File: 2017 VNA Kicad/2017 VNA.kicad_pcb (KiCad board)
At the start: 2 copper layers, 50 x 30 mm, 49 parts, among them P1 Output, P2 Input, U1 SI5351A, U2 NL7WB66, U3 NL7WB66, Y1 CX3225

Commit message: New PCB spin.
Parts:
- removed G***: Launchpad_LOGO_small, kilibs:Launchpad_LOGO_small
- removed G***: LOGO, EtherkitKicadLibrary:OSHWLogo4mm
- removed SHIELD1, SHIELD2: BMI-S-202-F, kilibs:LAIRD-BMI-S-202
- added ?: , RPi_Hat:RPi_Hat_Mounting_Hole, F.Cu at (111.5, 172.4)
- added ?: , RPi_Hat:RPi_Hat_Mounting_Hole, F.Cu at (111.5, 123.4)
- added ?: , RPi_Hat:RPi_Hat_Mounting_Hole, F.Cu at (53.5, 123.4)
- added ?: , RPi_Hat:RPi_Hat_Mounting_Hole, F.Cu at (53.5, 172.4)
- added A1: Arduino_Nano_v3.x, Modules:Arduino_Nano, F.Cu at (69.0, 144.0)
- added C11: 0.1uF, Capacitors_SMD:C_0805, F.Cu at (56.7, 148.3)
- added C18: 0.1uF, Capacitors_SMD:C_0805, F.Cu at (64.6, 129.5)
- added J1: AudioJack3, 2017 VNA Kicad:Tayda_3.5mm_stereo_TRS_jack_A-853, F.Cu at (56.0, 133.0)
- added J2: RF_Shield_Two_Pieces, kilibs:LAIRD-BMI-S-202, F.Cu at (65.0, 168.0)
- added J3: Raspberry_Pi_2_3, Pin_Headers:Pin_Header_Straight_2x20_Pitch2.54mm, F.Cu at (58.4, 124.7)
- added J4: RF_Shield_Two_Pieces, kilibs:LAIRD-BMI-S-202, F.Cu at (83.0, 168.0)
- added TX1: LO_Q, Connectors:PINTST, F.Cu at (48.2, 169.1)
- added U4: LM2904, 2017 VNA Kicad:SOIC-8, F.Cu at (83.0, 136.3)
- R3: value 56 -> 47
- moved U2 82.4 mm to (53.8, 162.6), turned to 0 degrees
- moved U3 77.5 mm to (111.6, 162.6), turned to 90 degrees
- moved B1 76.8 mm to (83.5, 148.4)
- moved C10 76.8 mm to (88.9, 159.8)
- moved C12 76.8 mm to (67.8, 156.8)
- moved C13 76.8 mm to (85.7, 154.6)
- moved C14 76.8 mm to (74.1, 156.1)
- moved C15 76.8 mm to (88.5, 153.1)
- moved C16 76.8 mm to (71.6, 152.8)
- moved C4 76.8 mm to (95.3, 164.9)
- moved C8 76.8 mm to (67.8, 162.3)
- moved CLK1 76.8 mm to (79.3, 165.0)
- moved IN1 76.8 mm to (97.7, 164.7)
- moved L1 76.8 mm to (67.7, 165.4)
- moved L2 76.8 mm to (87.7, 164.5)
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- renumbered LO_Q1 to CLK1
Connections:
- B1 pad 5V: (no net) -> +5V
- C1 pad 2: /Ref_In -> /TX
- C15 pad 1: Net-(B1-PadP5.1) -> Net-(C15-Pad1)
- C16 pad 1: Net-(B1-PadP4.7) -> Net-(C16-Pad1)
- C5 pad 1: +3V3 -> GND
- C5 pad 2: GND -> +3V3
- CLK1 pad 1: /LO_Q -> /Ref_In
- R15 pad 1: Net-(B1-PadP4.7) -> Net-(C16-Pad1)
- R8 pad 1: Net-(B1-PadP5.1) -> Net-(C15-Pad1)
- U1 pad 10: /Ref_In -> /TX
- U1 pad 9: /LO_Q -> /Ref_In
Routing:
- net +3V3: track 102.8 -> 79.4 mm
- net /TX: track 0.00 -> 15.1 mm
- net /Ref_In: track 15.1 -> 3.46 mm
- net Net-(B1-PadP5.1): track 21.2 -> 9.81 mm
- net GND: track 544.7 -> 535.0 mm, vias 196 -> 192
- net /SDA: track 46.8 -> 38.5 mm
- net /SCL: track 47.8 -> 40.9 mm
- net /LO_Q: track 3.46 -> 0.00 mm
- net Net-(B1-PadP4.7): track 21.6 -> 18.9 mm
- net /LO_I: vias 2 -> 3
- net Net-(C9-Pad1): vias 2 -> 3
- net (no net): vias 4 -> 5
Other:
- board size 50 x 30 mm -> 65 x 56 mm
- board text added: "Camera Flex Slot (Optional)"
- board text added: "Dimensions taken from https://github.com/raspberrypi/hats/blob/master/hat-board-mechanical.pdf"

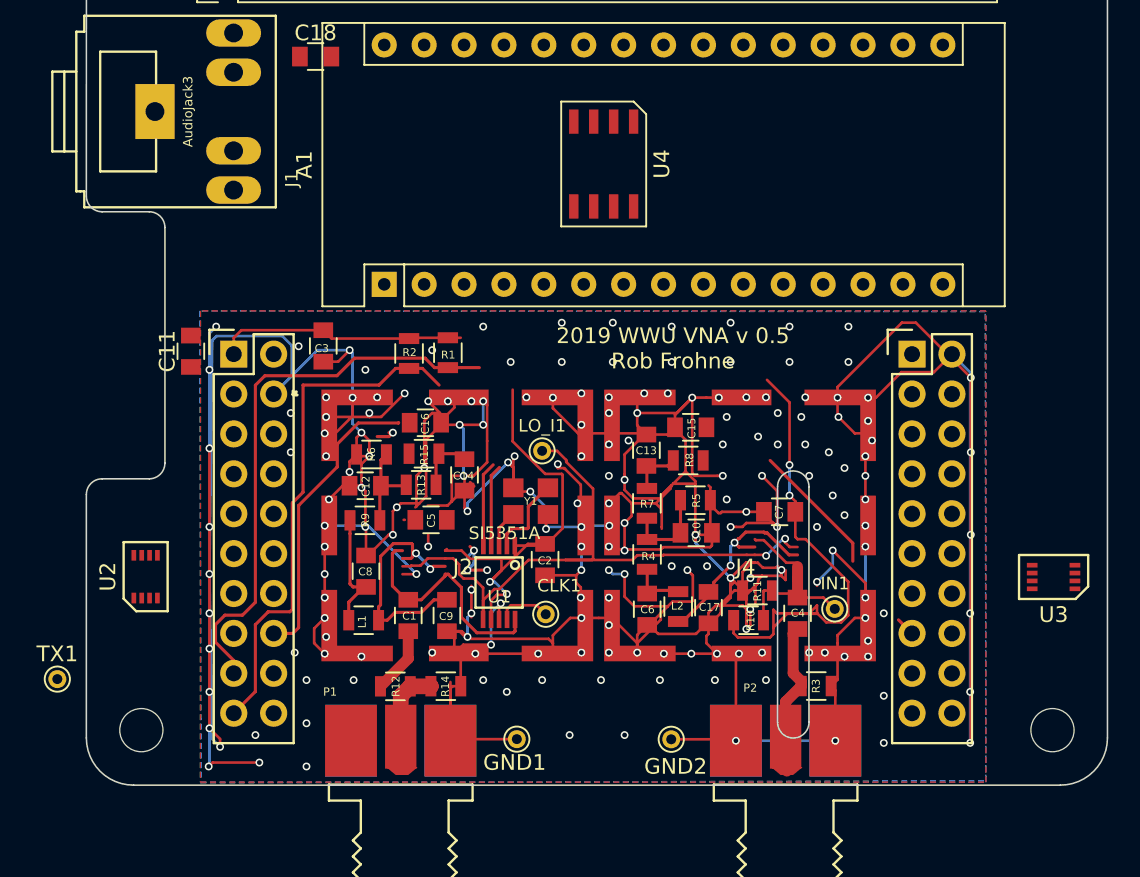
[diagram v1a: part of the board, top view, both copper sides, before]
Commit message: Added the footprint for the 3.5mm connector.
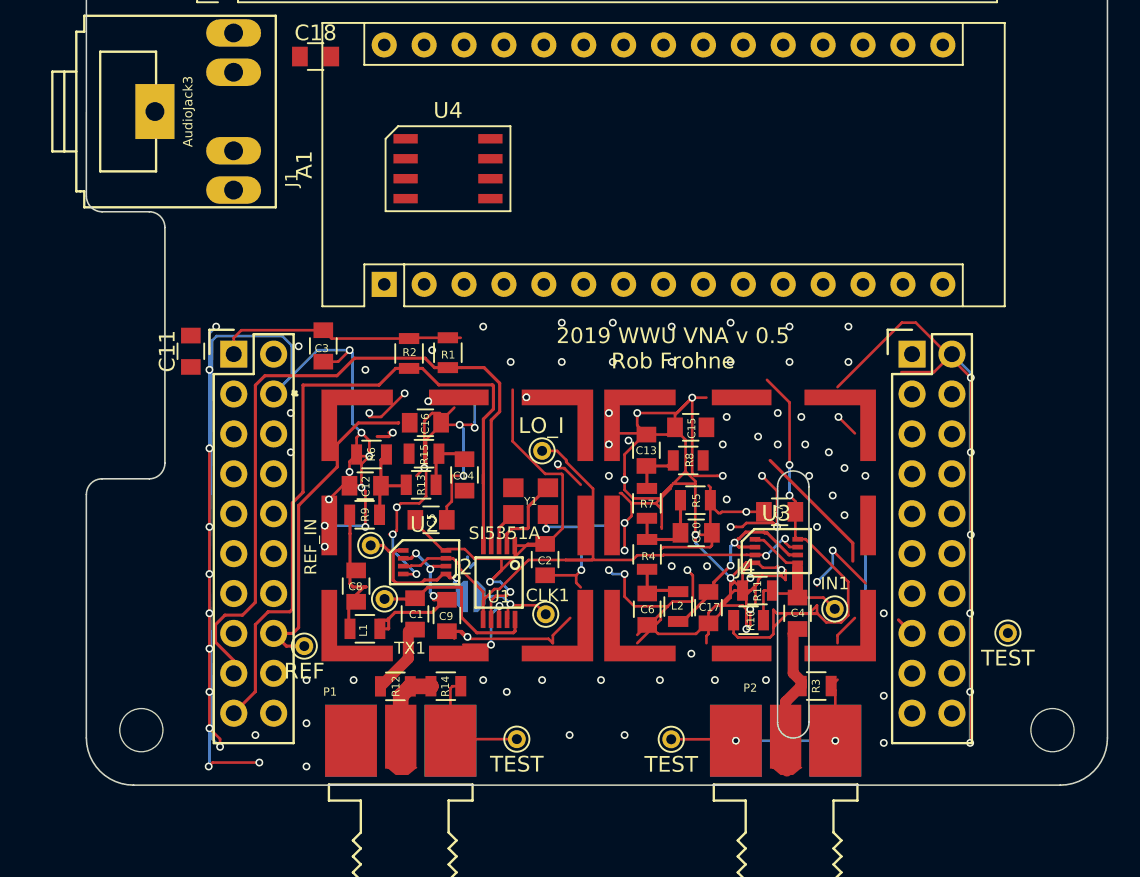
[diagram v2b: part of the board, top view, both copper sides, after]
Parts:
- added JP1: Jumper, EtherkitKicadLibrary:SOLDER_JUMPER, B.Cu at (74.5, 163.9)
- added TP1: REF_IN, Connectors:PINTST, F.Cu at (68.1, 160.6)
- added TP2: REF, Connectors:PINTST, F.Cu at (63.9, 167.0)
- added TP3: TEST, Connectors:PINTST, F.Cu at (108.7, 166.2)
- moved TX1 21.4 mm to (69.0, 164.0)
- moved U2 17.8 mm to (71.6, 161.7), turned to 270 degrees
- moved U3 17.7 mm to (94.0, 161.0), turned to 270 degrees
- moved U4 9.91 mm to (73.1, 136.6), turned to 270 degrees
- moved C8 1.14 mm to (67.2, 163.2)
- moved L1 0.55 mm to (67.8, 165.9)
- moved C1 0.44 mm to (71.0, 165.0)
- moved R9 0.35 mm to (67.8, 158.7)
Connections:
- CLK1 pad 1: /Ref_In -> Net-(CLK1-Pad1)
- J1 pad 1: (no net) -> GND
- J1 pad 2: (no net) -> Net-(B1-PadP5.1)
- J1 pad 3: (no net) -> Net-(B1-PadP4.7)
- U1 pad 9: /Ref_In -> Net-(CLK1-Pad1)
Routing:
- net GND: track 535.0 -> 411.0 mm, vias 192 -> 125
- net /SDA: track 38.5 -> 47.5 mm
- net /Ref_In: track 3.46 -> 10.8 mm, vias 0 -> 1
- net /SCL: track 40.9 -> 48.0 mm
- net Net-(CLK1-Pad1): track 0.00 -> 5.87 mm, vias 0 -> 1
- net (no net): track 5.05 -> 1.76 mm, vias 5 -> 2
- net +3V3: track 79.4 -> 82.6 mm
- net Net-(C9-Pad1): track 15.5 -> 12.6 mm
- net /TX: track 15.1 -> 12.8 mm
- net Net-(B1-PadP4.7): track 18.9 -> 21.2 mm
- net /LO_I: track 42.3 -> 41.9 mm, vias 3 -> 2
- removed copper zone on B.Cu, net GND
- removed copper zone on F.Cu, net GND

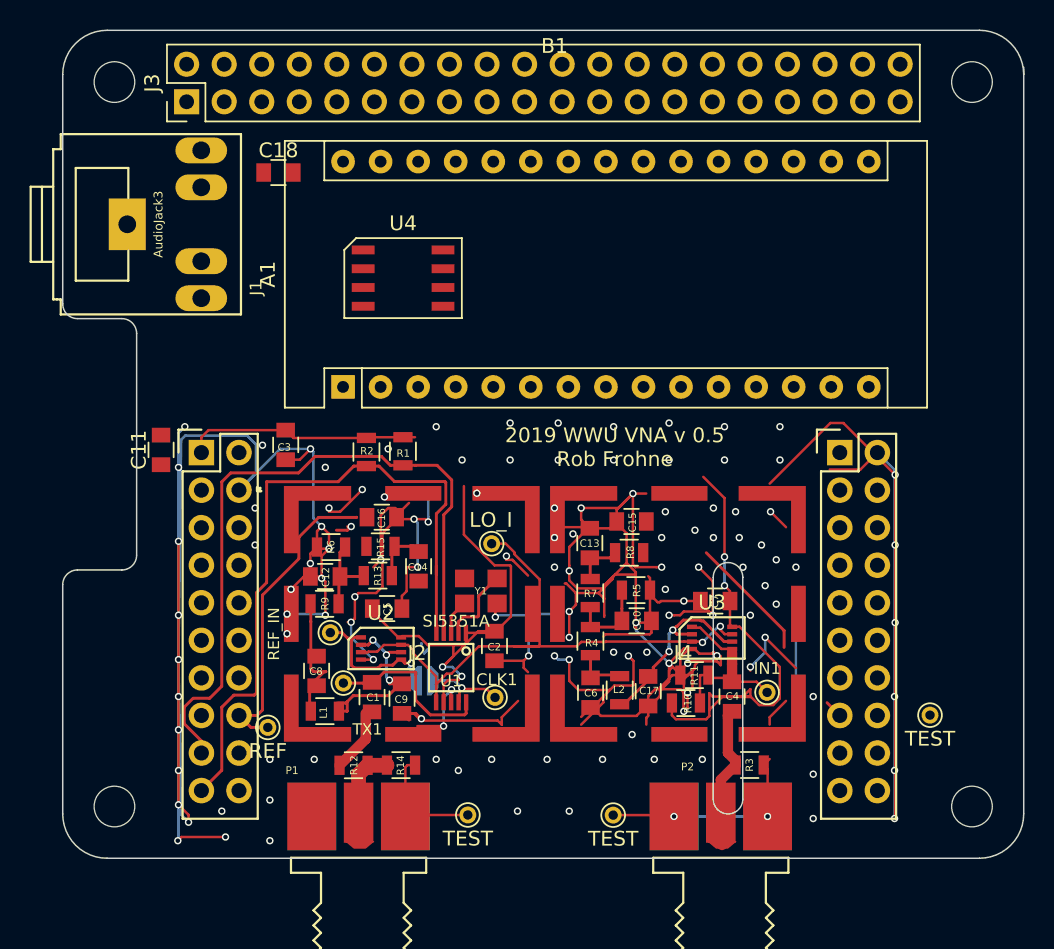
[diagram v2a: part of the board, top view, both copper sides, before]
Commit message: Added v0.51 to the Kicad directory.
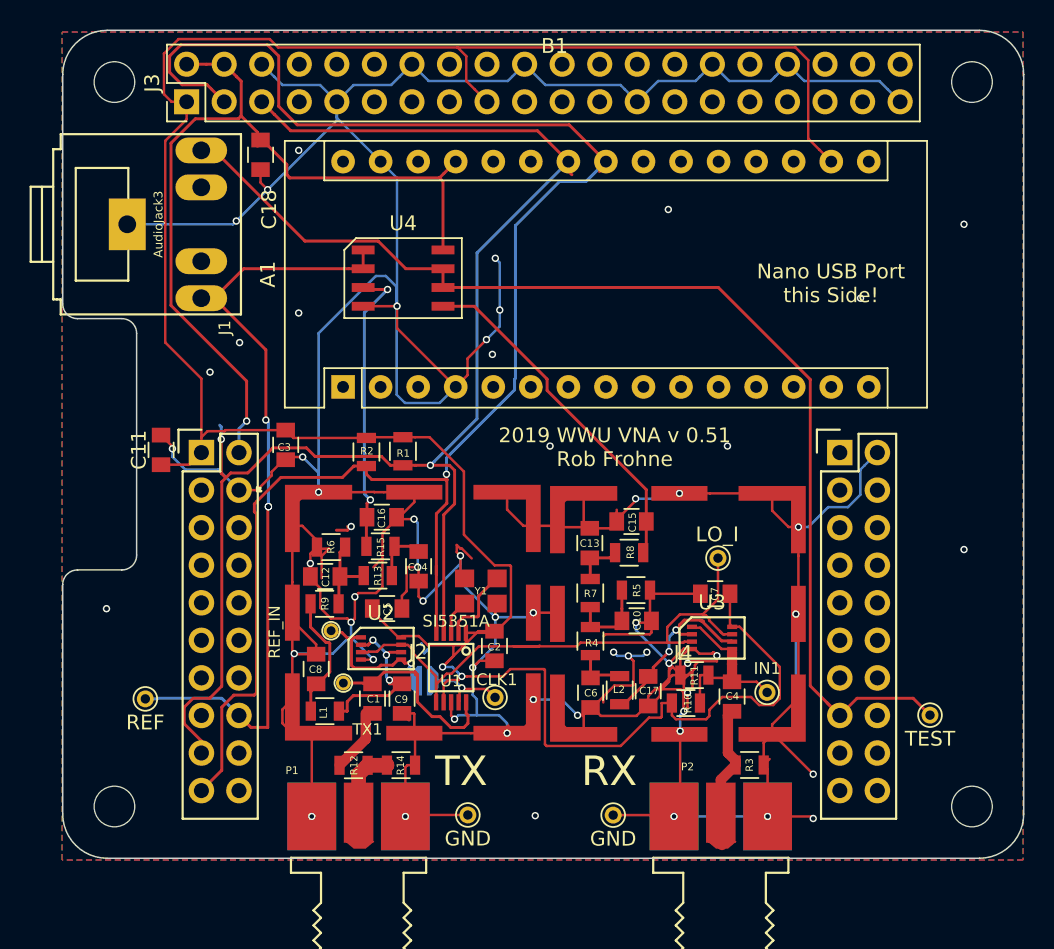
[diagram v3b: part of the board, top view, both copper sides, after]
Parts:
- GND1, GND2: value TEST -> GND
- moved LO_I1 15.3 mm to (94.4, 155.6)
- moved TP2 8.51 mm to (55.6, 165.1)
- moved C18 1.70 mm to (63.4, 128.3), turned to 270 degrees
- moved C7 0.49 mm to (94.2, 158.0)
- moved TP1 0.14 mm to (68.2, 160.5)
- moved C8 0.13 mm to (67.2, 163.1)
- moved J2 0.11 mm to (65.1, 167.9)
- moved C1 0.10 mm to (71.0, 165.1)
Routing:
- net +3V3: track 82.6 -> 181.7 mm, vias 4 -> 2
- net Net-(B1-PadP5.1): track 9.81 -> 80.2 mm
- net /SDA: track 47.5 -> 116.9 mm, vias 0 -> 1
- net +5V: track 0.00 -> 58.0 mm, vias 0 -> 1
- net /SCL: track 48.0 -> 100.7 mm, vias 0 -> 2
- net GND: track 411.0 -> 450.2 mm, vias 125 -> 57
- net Net-(B1-PadP4.7): track 21.2 -> 52.7 mm, vias 0 -> 3
- net Net-(C15-Pad1): track 0.00 -> 23.7 mm
- net Net-(C16-Pad1): track 0.00 -> 20.0 mm, vias 0 -> 2
- net /TX: track 12.8 -> 14.3 mm
- net /LO_I: track 41.9 -> 40.4 mm, vias 2 -> 0
- net Net-(C9-Pad1): track 12.6 -> 11.9 mm
- net Net-(C8-Pad1): track 7.79 -> 8.41 mm
- added copper zone on B.Cu, net GND
- added copper zone on F.Cu, net GND
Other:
- outline, holes or cut-outs redrawn
- board text added: "2019 WWU VNA v 0.51 Rob Frohne"
- board text added: "EXP-MSP432P401R or Arduino Nano or Raspberry Pi Vector Network Analyzer Booster Pack"
- board text added: "Nano USB Port this Side!"
- board text added: "RX"
- board text added: "TX"
- board text removed: "2019 WWU VNA v 0.5 Rob Frohne"
- board text removed: "EXP-MSP432P401R Vector Network Analyzer Booster Pack"
- board text removed: "https://github.com/frohro/WWU-VNA Made for ENGR 357 Walla Walla University, 2019 Rob Frohne"

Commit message: Hwi interrupt header testing....
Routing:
- net (no net): track 1.76 -> 0.41 mm, vias 2 -> 1
- net GND: track 450.2 -> 450.3 mm, vias 57 -> 58
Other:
- board text removed: "Camera Flex Slot (Optional)"
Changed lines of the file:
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@@
   (general
     (thickness 1.6)
-    (drawings 47)
-    (tracks 889)
+    (drawings 48)
+    (tracks 888)
     (zones 0)
     (modules 62)
     (nets 28)
   )
-  (page A4)
+  (page USLetter)
   (layers
     (0 F.Cu signal)
@@
     (44 Edge.Cuts user)
     (45 Margin user)
+    (46 B.CrtYd user)
     (47 F.CrtYd user)
-    (49 F.Fab user hide)
+    (49 F.Fab user)
   )
   (setup
@@
     (pad_to_mask_clearance 0.2)
     (solder_mask_min_width 0.25)
-    (pad_to_paste_clearance -0.05)
+    (pad_to_paste_clearance -0.07)
     (aux_axis_origin 0 0)
     (visible_elements FFFFFFFF)
@@
       (drillshape 0)
       (scaleselection 1)
-      (outputdirectory "Gerbers_v05_WWU_VNA_Rob"))
+      (outputdirectory "Gerbers_v05_1_WWU_VNA_Rob"))
   )
   (net 0 "")
@@
       (net 1 GND))
   )
+  (dimension 56 (width 0.15) (layer Dwgs.User)
+    (gr_text "2.2047 in" (at 129.3 148 90) (layer Dwgs.User)
+      (effects (font (size 1 1) (thickness 0.15)))
+    )
+    (feature1 (pts (xy 115 120) (xy 128.586421 120)))
+    (feature2 (pts (xy 115 176) (xy 128.586421 176)))
+    (crossbar (pts (xy 128 176) (xy 128 120)))
+    (arrow1a (pts (xy 128 120) (xy 128.586421 121.126504)))
+    (arrow1b (pts (xy 128 120) (xy 127.413579 121.126504)))
+    (arrow2a (pts (xy 128 176) (xy 128.586421 174.873496)))
+    (arrow2b (pts (xy 128 176) (xy 127.413579 174.873496)))
+  )
+  (dimension 65 (width 0.15) (layer Dwgs.User)
+    (gr_text "2.5591 in" (at 82.5 194.3) (layer Dwgs.User)
+      (effects (font (size 1 1) (thickness 0.15)))
+    )
+    (feature1 (pts (xy 115 176) (xy 115 193.586421)))
+    (feature2 (pts (xy 50 176) (xy 50 193.586421)))
+    (crossbar (pts (xy 50 193) (xy 115 193)))
+    (arrow1a (pts (xy 115 193) (xy 113.873496 193.586421)))
+    (arrow1b (pts (xy 115 193) (xy 113.873496 192.413579)))
+    (arrow2a (pts (xy 50 193) (xy 51.126504 193.586421)))
+    (arrow2b (pts (xy 50 193) (xy 51.126504 192.413579)))
+  )
   (gr_text RX (at 87 170) (layer F.SilkS)
     (effects (font (size 2 2) (thickness 0.15)))
@@
   (gr_arc (start 51.038 138.38) (end 51.038 139.38) (angle 90) (layer Edge.Cuts) (width 0.1))
   (gr_arc (start 53.038 172.88) (end 53.038 175.88) (angle 90) (layer Edge.Cuts) (width 0.1))
-  (gr_text "Camera Flex Slot\n(Optional)" (at 94.788 179.63) (layer Cmts.User)
-    (effects (font (size 1.5 1.5) (thickness 0.15)))
-  )
   (gr_text "Dimensions taken from\nhttps://github.com/raspberrypi/hats/blob/master/hat-board-mechanical.pdf" (at 86.538 186.38) (layer Cmts.User)
     (effects (font (size 1.5 1.5) (thickness 0.15) italic))
@@
     (arrow2b (pts (xy 129 70) (xy 129.586421 71.126504)))
   )
-  (via (at 69.55 153.442) (size 0.5) (drill 0.3) (layers F.Cu B.Cu) (net 0))
-  (segment (start 68.55 153.692) (end 69.3 153.692) (width 0.2) (layer F.Cu) (net 0))
-  (segment (start 69.3 153.692) (end 69.55 153.442) (width 0.2) (layer F.Cu) (net 0))
-  (segment (start 69.55 153.442) (end 69.3 153.442) (width 0.2) (layer F.Cu) (net 0))
   (segment (start 74.3 161.442) (end 74.3 161.351998) (width 0.2) (layer B.Cu) (net 0))
   (segment (start 74.705901 161.782002) (end 74.486956 162.000947) (width 0.2) (layer B.Cu) (net 0))
@@
   (via (at 111 133) (size 0.5) (drill 0.3) (layers F.Cu B.Cu) (net 1))
   (via (at 83 148) (size 0.5) (drill 0.3) (layers F.Cu B.Cu) (net 1))
+  (segment (start 68.05 154.942) (end 68.05 154.942) (width 0.7) (layer F.Cu) (net 1))
+  (segment (start 68.05 154.942) (end 67.996 154.996) (width 0.7) (layer F.Cu) (net 1))
+  (via (at 68.05 154.942) (size 0.5) (drill 0.3) (layers F.Cu B.Cu) (net 1))
   (segment (start 70.98 159.18) (end 70.98 158.992) (width 0.17) (layer F.Cu) (net 2) (status 30))
   (segment (start 72.74 160.94) (end 70.98 159.18) (width 0.17) (layer F.Cu) (net 2) (status 30))

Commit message: updated the pcb...
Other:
- rule pad_to_mask_clearance: 0.2 -> 0

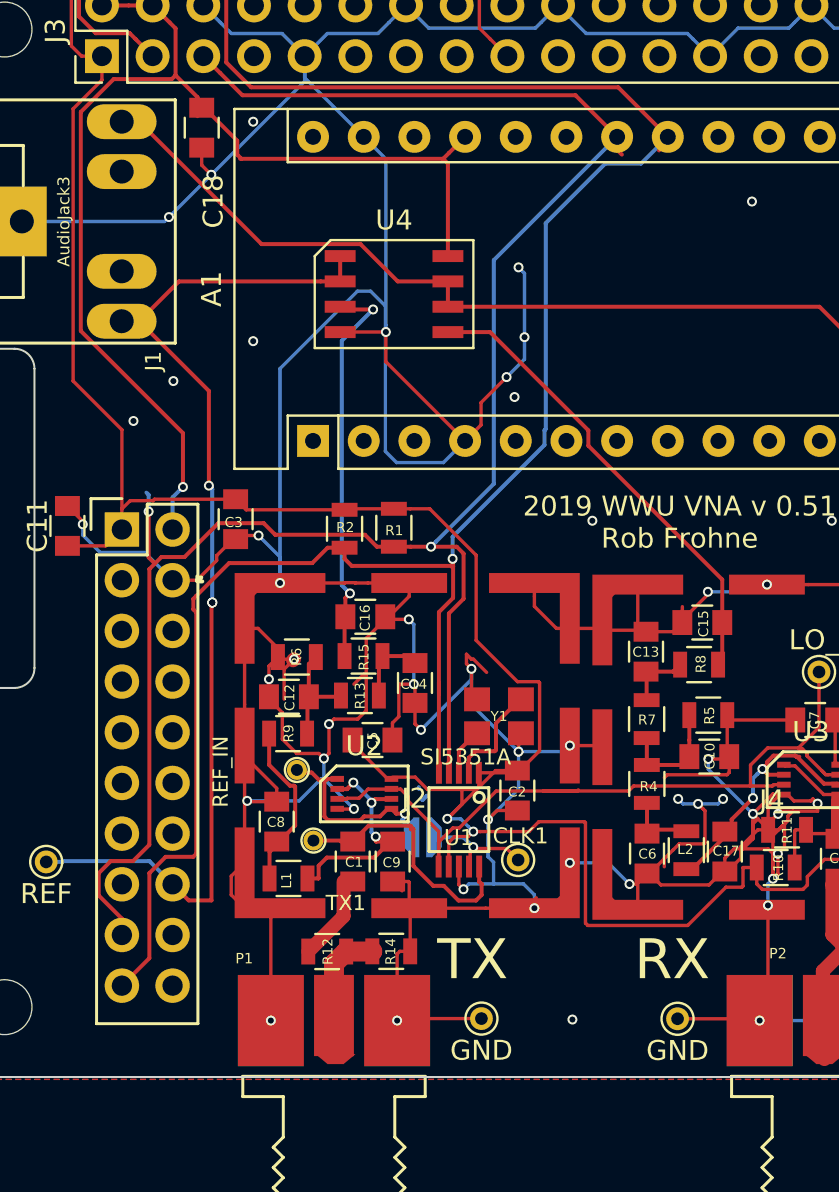
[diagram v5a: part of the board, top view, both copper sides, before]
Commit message: Updated the netlest and PCB for v0.52 (180 ohm current sink).
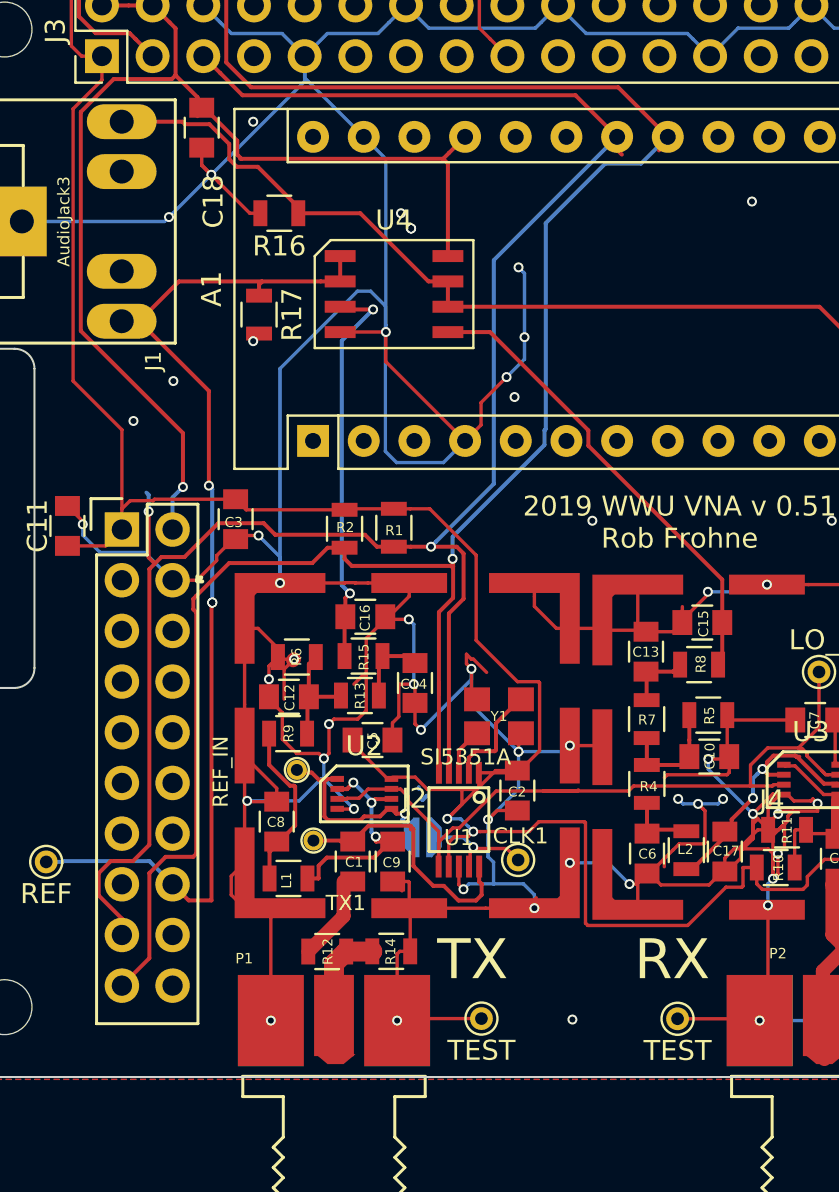
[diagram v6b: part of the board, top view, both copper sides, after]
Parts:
- added R16: 180, Resistors_SMD:R_0805, F.Cu at (67.3, 132.6)
- added R17: 180, Resistors_SMD:R_0805, F.Cu at (66.3, 137.7)
- GND1, GND2: value GND -> TEST
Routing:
- net GND: track 450.3 -> 454.8 mm, vias 58 -> 61
- net Net-(B1-PadP4.7): track 52.7 -> 53.5 mm
- net Net-(B1-PadP5.1): track 80.2 -> 80.8 mm
